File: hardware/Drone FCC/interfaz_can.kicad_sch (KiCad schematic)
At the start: 4 parts, among them J17 CAN 1, J18 CAN 2, U4 SN65HVD230, U5 SN65HVD230

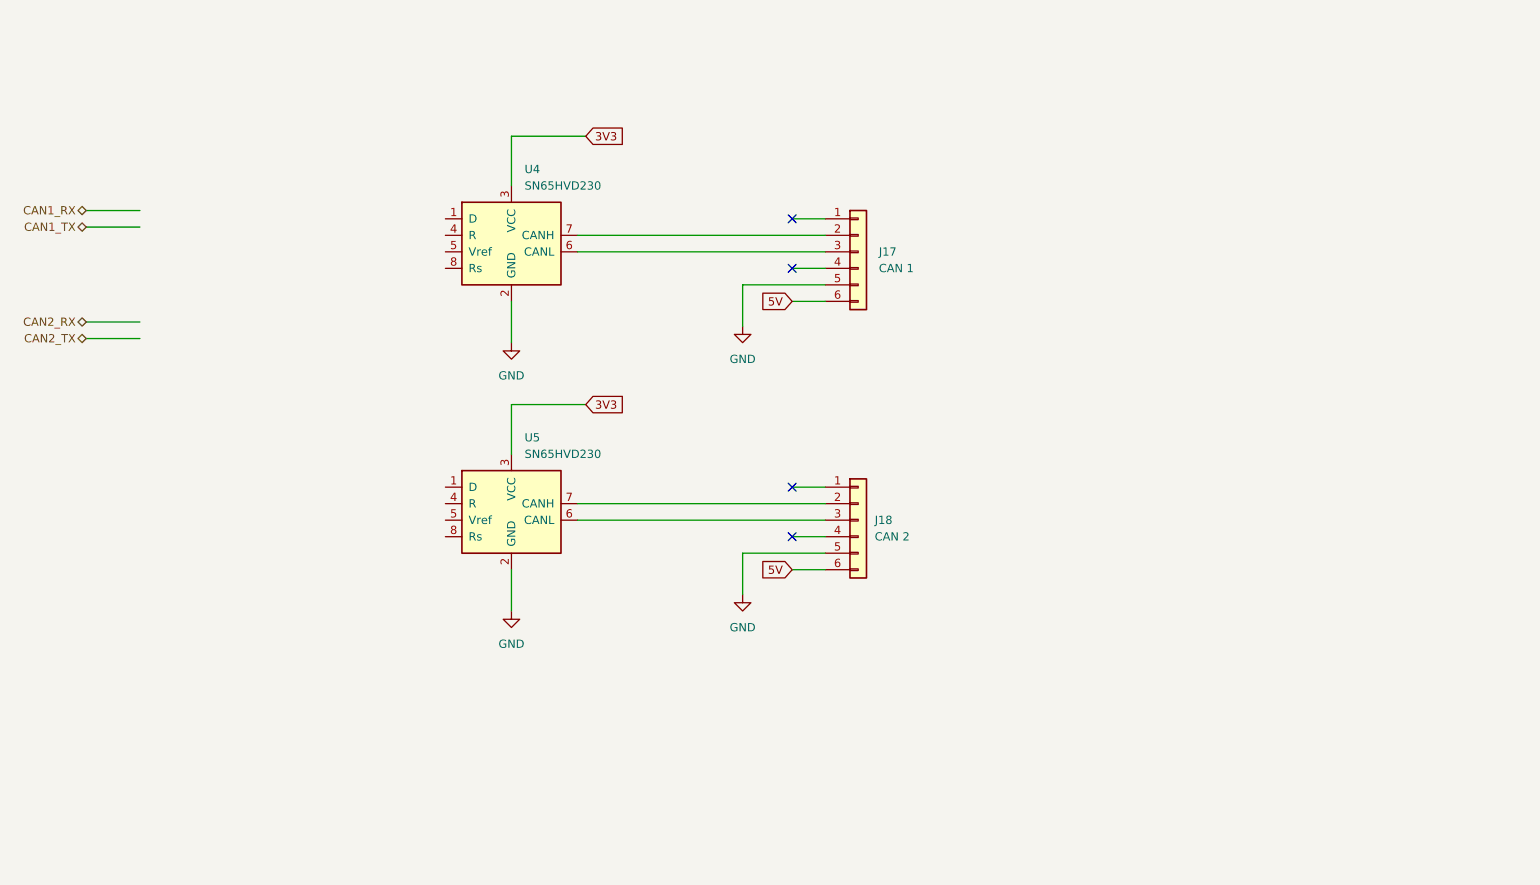
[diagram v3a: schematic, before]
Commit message: add CAN schematic
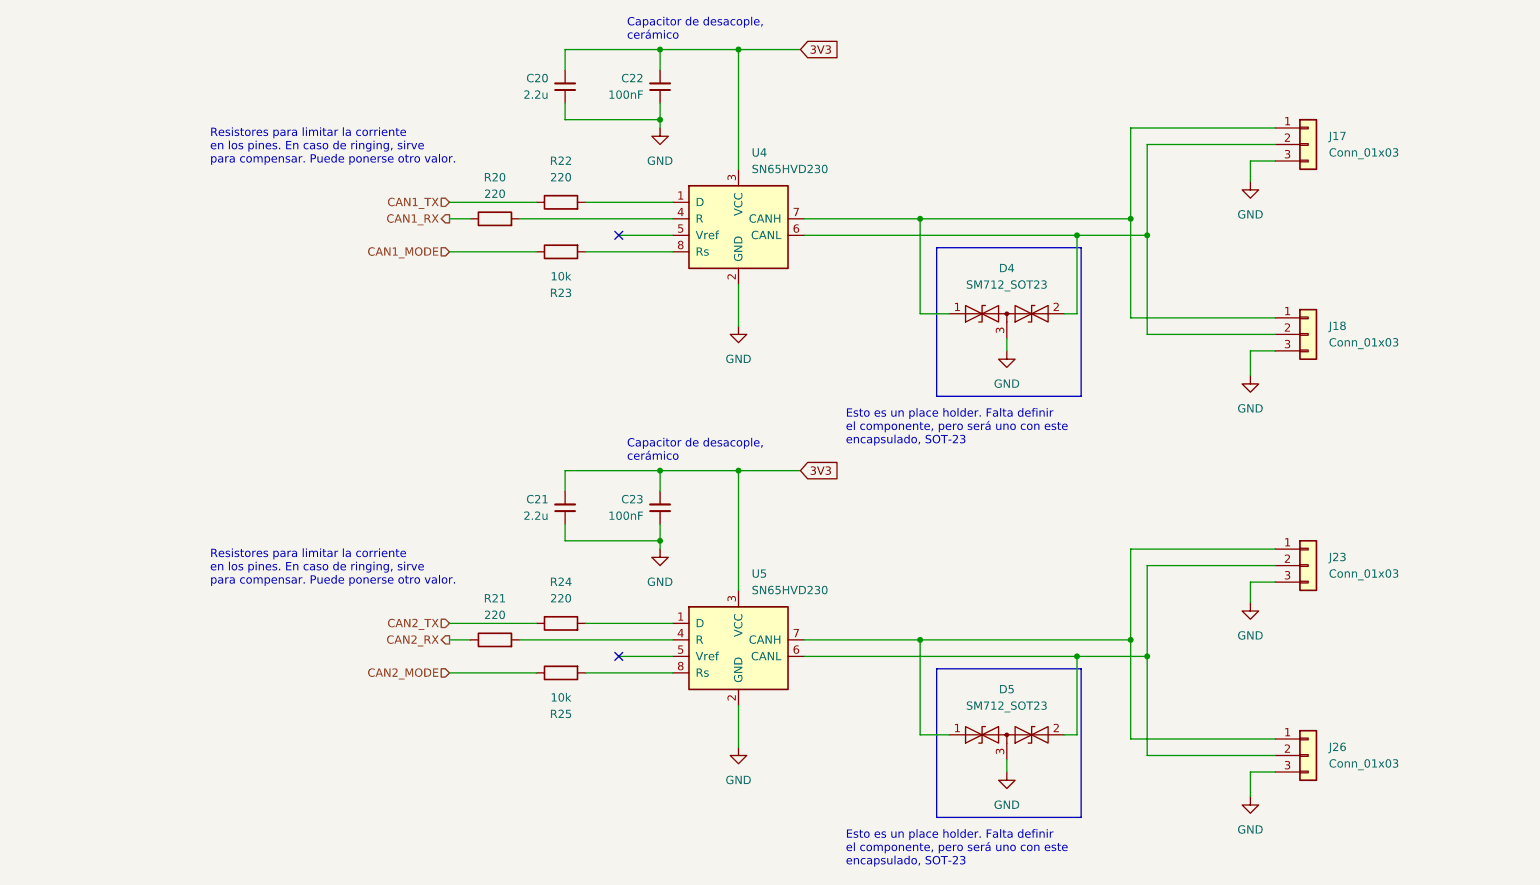
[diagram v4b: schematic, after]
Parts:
- removed J17: CAN 1, Connector_Molex:Molex_Micro-Fit_3.0_43045-0600_2x03_P3.00mm_Horizontal, symbol Connector_Generic:Conn_01x06
- removed J18: CAN 2, Connector_Molex:Molex_Micro-Fit_3.0_43045-0600_2x03_P3.00mm_Horizontal, symbol Connector_Generic:Conn_01x06
- added C20, C21: 2.2u, symbol Device:C_Small
- added C22, C23: 100nF, symbol Device:C_Small
- added D4, D5: SM712_SOT23, Package_TO_SOT_SMD:SOT-23, symbol Diode:SM712_SOT23
- added J17, J18, J23, J26: Conn_01x03, DF13A-3P-1.25H(21):HRS_DF13A-3P-1.25H(21), symbol Connector_Generic:Conn_01x03
- added R20, R21, R22, R24: 220, symbol Device:R
- added R23, R25: 10k, symbol Device:R
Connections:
- net 3V3: now also C20.2, C21.2, C22.2, C23.2
- net CAN1_RX: now also R20.1
- net CAN1_TX: now also R22.1
- net CAN2_RX: now also R21.1
- net CAN2_TX: now also R24.1
- net GND: now also C20.1, C21.1, C22.1, C23.1, D4.3 (common), D5.3 (common), J17.3 (Pin_3), J18.3 (Pin_3), J23.3 (Pin_3), J26.3 (Pin_3)
- net at U4.1 (D): now also R22.2
- net at U4.4 (R): now also R20.2
- net at U4.6 (CANL): now also D4.2 (A2), J17.2 (Pin_2), J18.2 (Pin_2)
- net at U4.7 (CANH): now also D4.1 (A1), J17.1 (Pin_1), J18.1 (Pin_1)
- net at U4.8 (Rs): now also R23.2
- net at U5.1 (D): now also R24.2
- net at U5.4 (R): now also R21.2
- net at U5.6 (CANL): now also D5.2 (A2), J23.2 (Pin_2), J26.2 (Pin_2)
- net at U5.7 (CANH): now also D5.1 (A1), J23.1 (Pin_1), J26.1 (Pin_1)
- net at U5.8 (Rs): now also R25.2
- new net CAN1_MODE: R23.1
- new net CAN2_MODE: R25.1
- no-connect marks 4 -> 2
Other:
- note added: "Capacitor de desacople, cerámico"
- note added: "Esto es un place holder. Falta definir el componente, pero será uno con este encapsulado, SOT-23"
- note added: "Resistores para limitar la corriente en los pines. En caso de ringing, sirve para compensar. Puede ponerse otro valor."
- moved on the sheet: U4

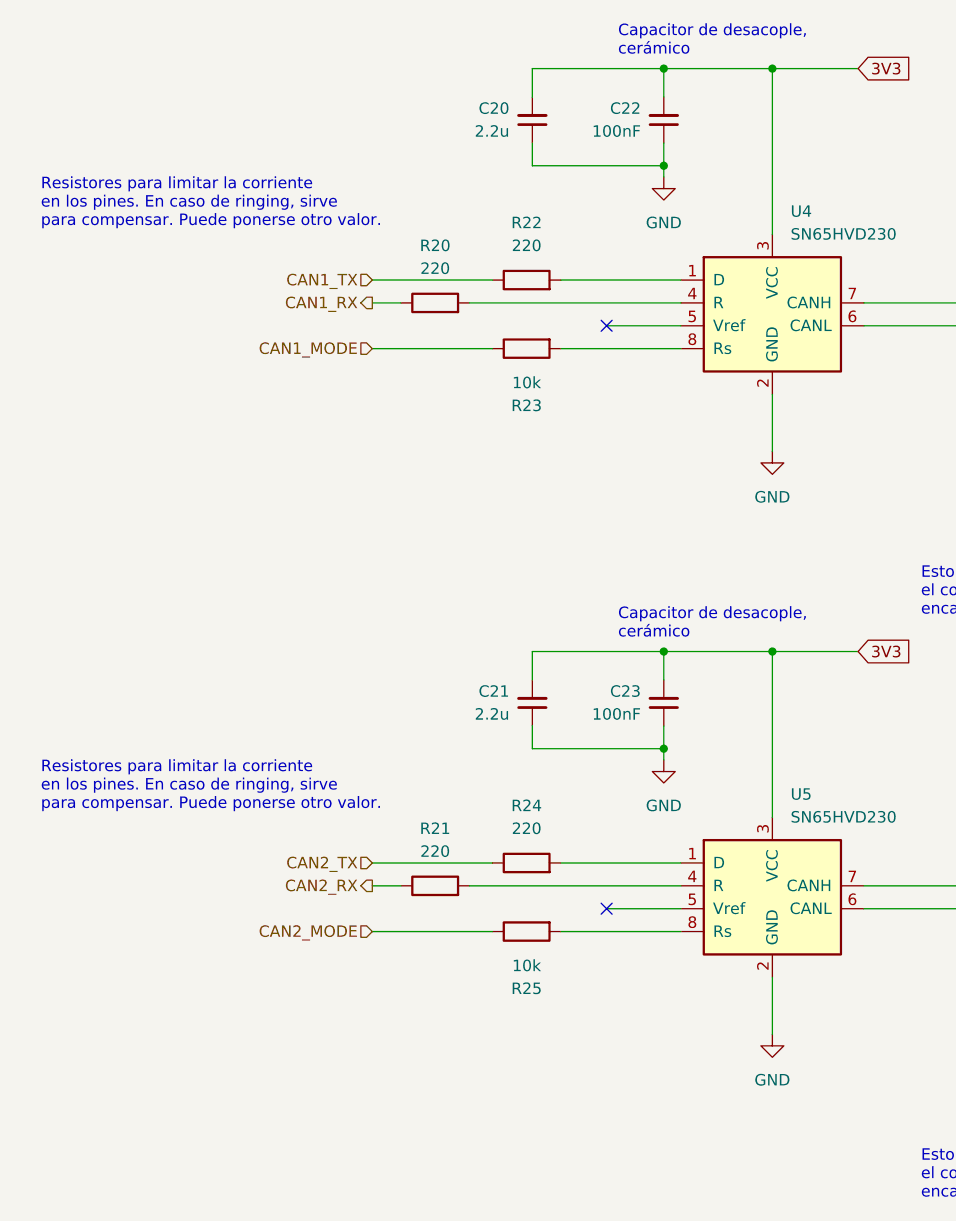
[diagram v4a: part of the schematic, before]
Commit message: add external communication connectors
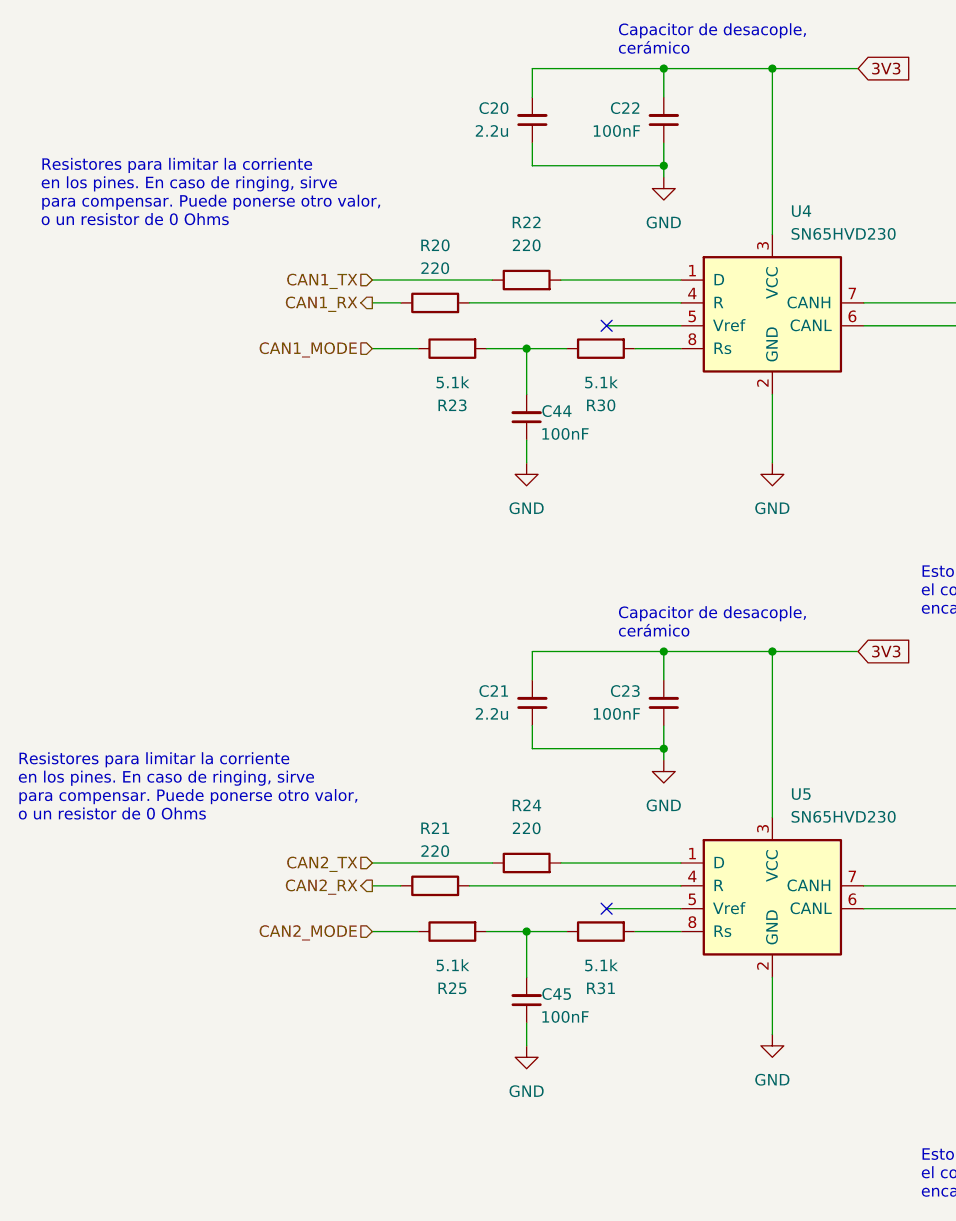
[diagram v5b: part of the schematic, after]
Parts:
- added C44, C45: 100nF, symbol Device:C_Small
- added R30, R31: 5.1k, symbol Device:R
- R23, R25: value 10k -> 5.1k
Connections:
- net GND: now also C44.1, C45.1
- net at U4.8 (Rs): now also R30.2; no longer R23.2
- net at U5.8 (Rs): now also R31.2; no longer R25.2
- new net: C44.2, R23.2, R30.1
- new net: C45.2, R25.2, R31.1
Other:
- note added: "Resistores para limitar la corriente en los pines. En caso de ringing, sirve para compensar. Puede ponerse otro valor, o un resistor de 0 Ohms"
- note removed: "Resistores para limitar la corriente en los pines. En caso de ringing, sirve para compensar. Puede ponerse otro valor."
- moved on the sheet: R23
